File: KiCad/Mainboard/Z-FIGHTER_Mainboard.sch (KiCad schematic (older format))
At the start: 44 parts, among them IC1 Z80SIO, J1 DB9_Male_MountingHoles, J2 DB9_Male_MountingHoles, J3 USB_B, J4 Conn_02x13_Odd_Even, J5 Conn_Parallel_User, J6 Conn_PATA, J7 Conn_02x03_Odd_Even, SW1 SW_Push, SW2 SW_DIP_x03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

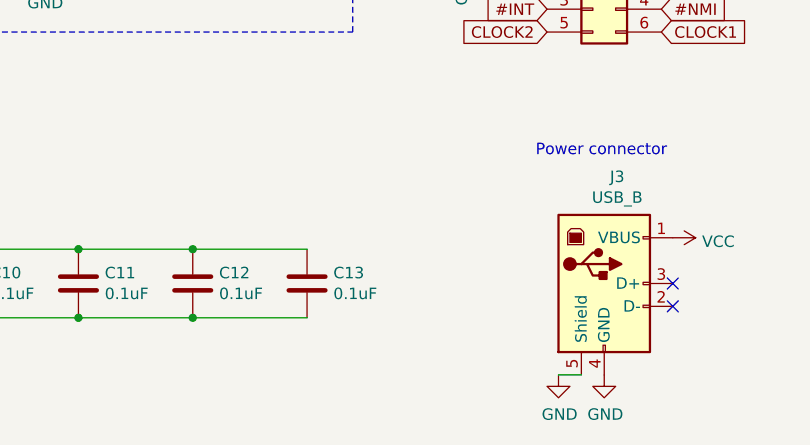
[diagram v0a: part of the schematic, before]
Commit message: Fixed bypass
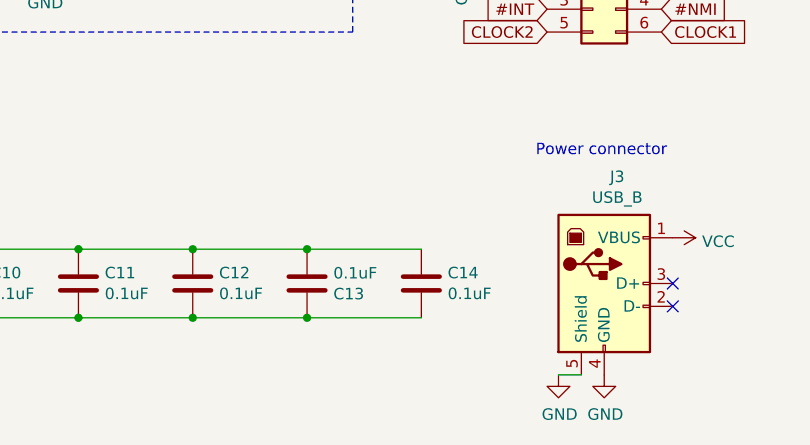
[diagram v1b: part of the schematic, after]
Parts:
- added C14: 0.1uF, Capacitor_THT:C_Disc_D7.5mm_W2.5mm_P5.00mm, symbol Device:C
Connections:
- net GND: now also C13.1, C14.2; no longer C13.2
- net VCC: now also C13.2, C14.1; no longer C13.1
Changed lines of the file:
@@
 	1    0    0    -1
 $EndComp
-$Comp
-L Device:C C13
-U 1 1 603D9D9B
-P 8600 10000
-F 0 "C13" H 8715 10046 50  0000 L CNN
-F 1 "0.1uF" H 8715 9955 50  0000 L CNN
-F 2 "Capacitor_THT:C_Disc_D7.5mm_W2.5mm_P5.00mm" H 8638 9850 50  0001 C CNN
-F 3 "~" H 8600 10000 50  0001 C CNN
-	1    8600 10000
-	1    0    0    -1
-$EndComp
-Connection ~ 8100 9850
-Wire Wire Line
-	8100 9850 8600 9850
 Connection ~ 8100 10150
 Wire Wire Line
@@
 Text Notes 4700 950  0    50   ~ 0
 SRAM
+Connection ~ 8100 9850
+Wire Wire Line
+	8100 9850 8600 9850
+$Comp
+L Device:C C13
+U 1 1 603D9D9B
+P 8600 10000
+F 0 "C13" H 8715 10046 50  0000 L CNN
+F 1 "0.1uF" H 8715 9955 50  0000 L CNN
+F 2 "Capacitor_THT:C_Disc_D7.5mm_W2.5mm_P5.00mm" H 8638 9850 50  0001 C CNN
+F 3 "~" H 8600 10000 50  0001 C CNN
+	1    8600 10000
+	1    0    0    1
+$EndComp
+$Comp
+L Device:C C14
+U 1 1 614E6A45
+P 9100 10000
+F 0 "C14" H 9215 10046 50  0000 L CNN
+F 1 "0.1uF" H 9215 9955 50  0000 L CNN
+F 2 "Capacitor_THT:C_Disc_D7.5mm_W2.5mm_P5.00mm" H 9138 9850 50  0001 C CNN
+F 3 "~" H 9100 10000 50  0001 C CNN
+	1    9100 10000
+	1    0    0    -1
+$EndComp
+Wire Wire Line
+	8600 9850 9100 9850
+Connection ~ 8600 9850
+Wire Wire Line
+	8600 10150 9100 10150
+Connection ~ 8600 10150
 $EndSCHEMATC

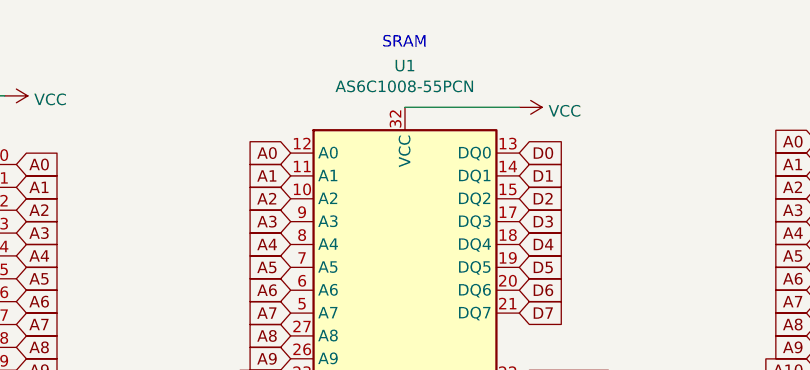
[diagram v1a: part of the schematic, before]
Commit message: Changed SRAM silkscreen back to '4008
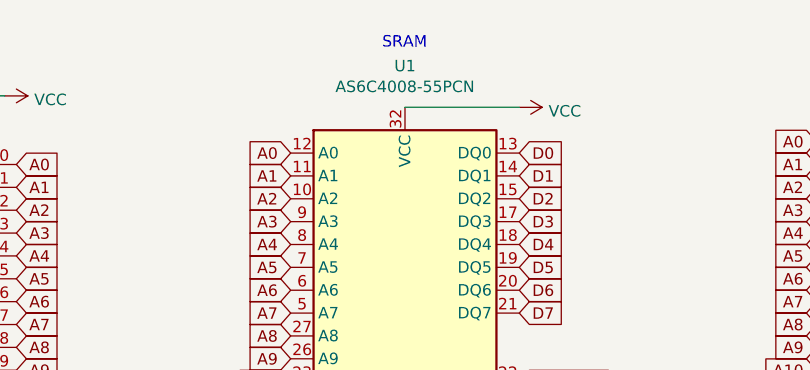
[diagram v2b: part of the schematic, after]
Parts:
- U1: value AS6C1008-55PCN -> AS6C4008-55PCN
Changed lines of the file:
@@
 P 4800 2300
 F 0 "U1" H 4800 3581 50  0000 C CNN
-F 1 "AS6C1008-55PCN" H 4800 3490 50  0000 C CNN
+F 1 "AS6C4008-55PCN" H 4800 3490 50  0000 C CNN
 F 2 "Package_DIP:DIP-32_W15.24mm" H 4800 2400 50  0001 C CNN
 F 3 "https://www.alliancememory.com/wp-content/uploads/pdf/AS6C4008.pdf" H 4800 2400 50  0001 C CNN
